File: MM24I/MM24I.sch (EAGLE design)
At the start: 32 parts, among them IC1 SN74LVC2G17DBVR, IC2 SN74LVC14APWR, U1 SN74LVCH16374ADGGR, U2 SN74LVCH16374ADGGR, U3 CY14B104M, U4 SN74AHCT16373DGGR, U5 TLV803SDBZ

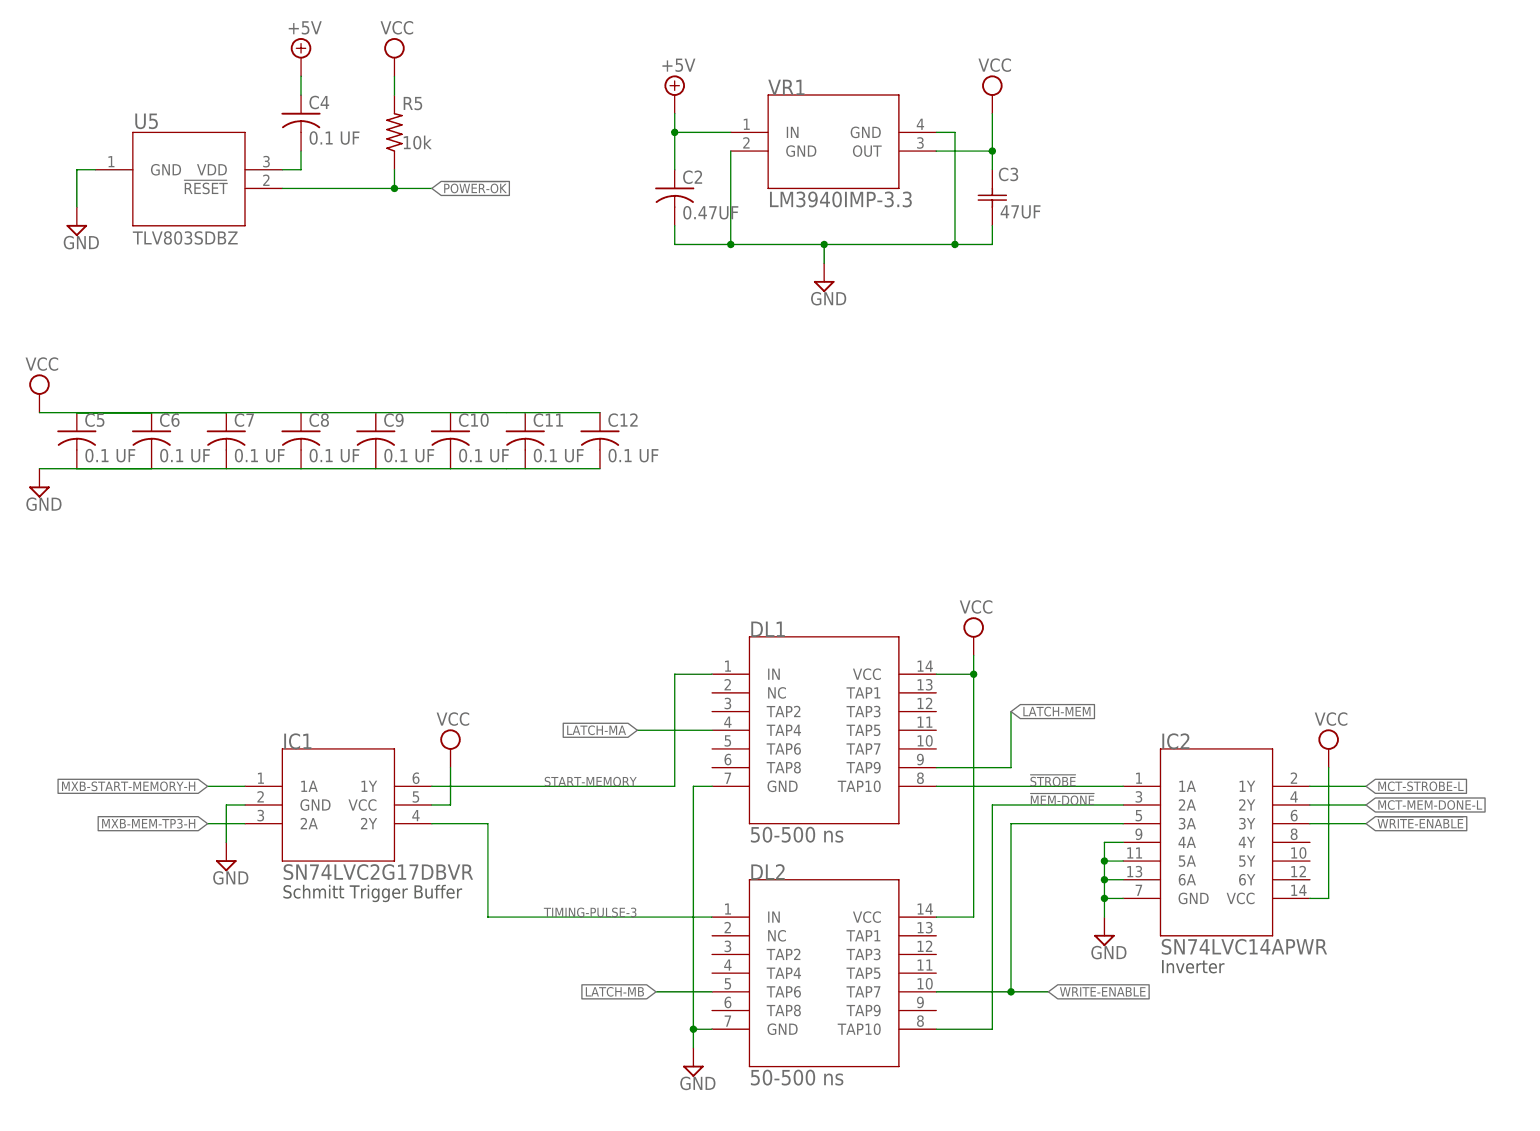
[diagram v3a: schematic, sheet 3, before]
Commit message: Added bypass capacitors, reworked W021J
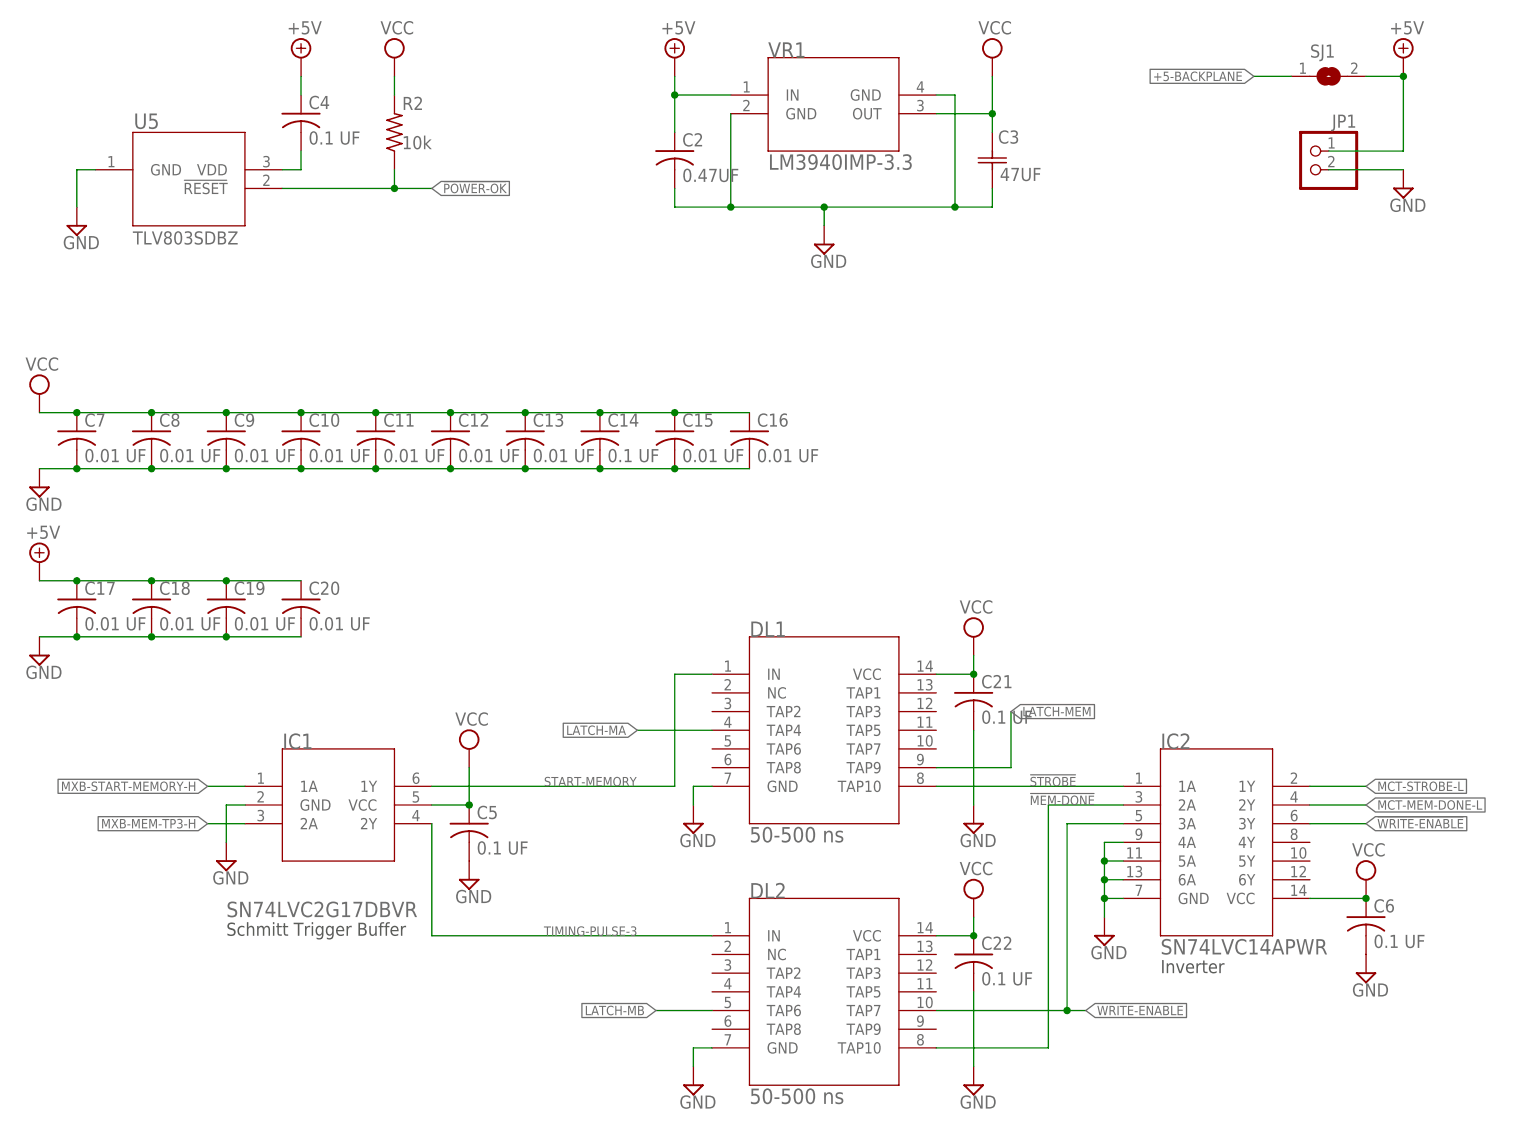
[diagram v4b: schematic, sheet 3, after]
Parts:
- removed R3, R4, R5: 10k, rcl:R-US_R1206
- added C13, C15, C16, C17, C18, C19, C20: 0.01 UF, rcl:C-USC0402
- added C14, C21, C22: 0.1 UF, rcl:C-USC0402
- added JP1: (no value), pinhead:PINHD-1X2
- added SJ1: (no value), jumper:SJ
- C10, C11, C12, C7, C8, C9: value 0.1 UF -> 0.01 UF; device rcl:C-USC0805 -> rcl:C-USC0402
- C4, C5, C6: device rcl:C-USC0805 -> rcl:C-USC0402
- R1, R2: device rcl:R-US_R1206 -> rcl:R-US_R0402
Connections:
- removed net N$10: R2.2, U3.DQ14
- removed net N$12: R3.2, U3.DQ13
- removed net N$8: R4.2, U3.DQ12
- new net +5-BACKPLANE: SJ1.1, U$1A2.1
- net !POWER-OK: now also R2.1; no longer R5.1
- net +5V: now also C17.1, C18.1, C19.1, C20.1, JP1.1, SJ1.2
- net GND: now also C13.2, C14.2, C15.2, C16.2, C17.2, C18.2, C19.2, C20.2, C21.2, C22.2, JP1.2; no longer R2.1, R3.1, R4.1
- net N$9: now also U3.DQ12, U3.DQ13, U3.DQ14
- net VCC: now also C13.1, C14.1, C15.1, C16.1, C21.1, C22.1, R2.2; no longer R5.2
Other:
- moved on the sheet: C10, C11, C12, C2, C3, C5, C6, C7, C8, C9, DL2, VR1

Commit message: Rework MM24I voltage supervisor
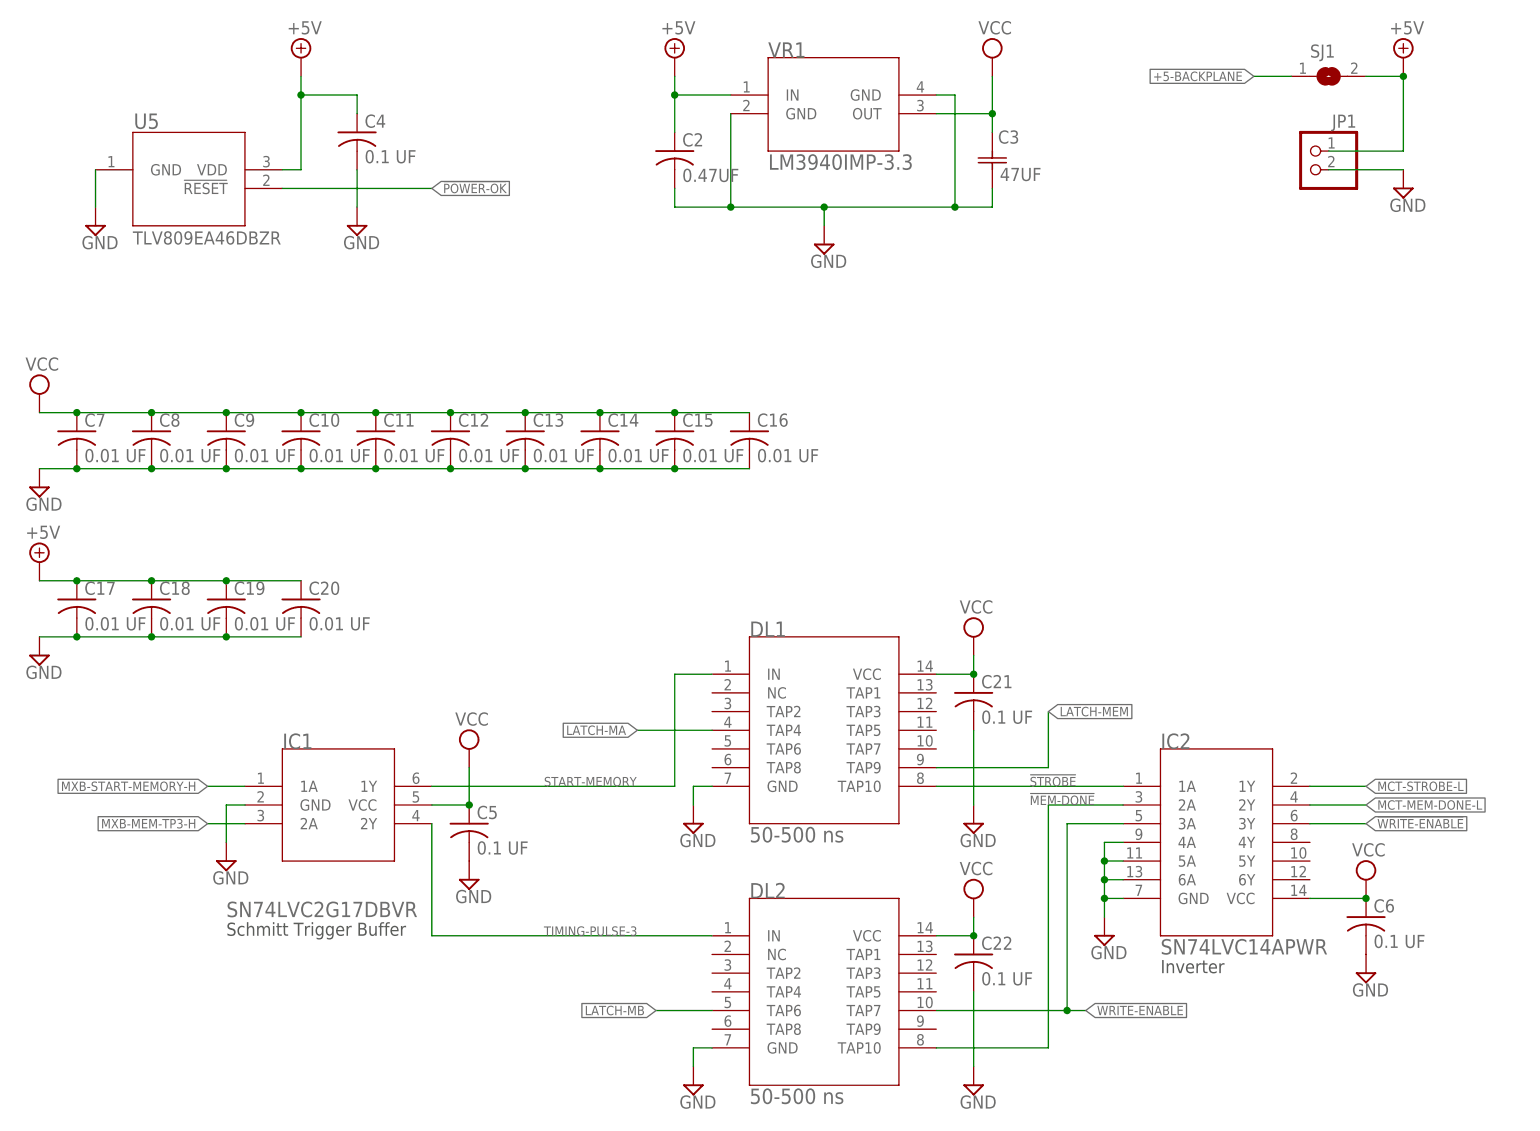
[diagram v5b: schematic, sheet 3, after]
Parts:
- removed R2: 10k, rcl:R-US_R0402
- C14: value 0.1 UF -> 0.01 UF
- U5: value TLV803SDBZ -> TLV809EA46DBZR; device MM24I:TLV803SDBZ -> MM24I:TLV809EA46DBZR
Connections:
- removed net N$1: C4.2, U5.VDD
- net !POWER-OK: no longer R2.1
- net +5V: now also U5.VDD
- net GND: now also C4.2
- net VCC: no longer R2.2
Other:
- moved on the sheet: C4
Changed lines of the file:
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@@
 <part name="U$1" library="dec-con" deviceset="SINGLE" device=""/>
 <part name="SUPPLY23" library="supply2" library_urn="urn:adsk.eagle:library:372" deviceset="GND" device=""/>
-<part name="SUPPLY27" library="supply2" library_urn="urn:adsk.eagle:library:372" deviceset="VCC" device=""/>
-<part name="U5" library="MM24I" deviceset="TLV803SDBZ" device=""/>
-<part name="R2" library="rcl" library_urn="urn:adsk.eagle:library:334" deviceset="R-US_" device="R0402" package3d_urn="urn:adsk.eagle:package:23547/3" value="10k"/>
+<part name="U5" library="MM24I" deviceset="TLV809EA46DBZR" device=""/>
 <part name="SUPPLY28" library="supply2" library_urn="urn:adsk.eagle:library:372" deviceset="+5V" device=""/>
 <part name="C4" library="rcl" library_urn="urn:adsk.eagle:library:334" deviceset="C-US" device="C0402" package3d_urn="urn:adsk.eagle:package:23626/2" value="0.1 UF"/>
@@
 <part name="C12" library="rcl" library_urn="urn:adsk.eagle:library:334" deviceset="C-US" device="C0402" package3d_urn="urn:adsk.eagle:package:23626/2" value="0.01 UF"/>
 <part name="C13" library="rcl" library_urn="urn:adsk.eagle:library:334" deviceset="C-US" device="C0402" package3d_urn="urn:adsk.eagle:package:23626/2" value="0.01 UF"/>
-<part name="C14" library="rcl" library_urn="urn:adsk.eagle:library:334" deviceset="C-US" device="C0402" package3d_urn="urn:adsk.eagle:package:23626/2" value="0.1 UF"/>
+<part name="C14" library="rcl" library_urn="urn:adsk.eagle:library:334" deviceset="C-US" device="C0402" package3d_urn="urn:adsk.eagle:package:23626/2" value="0.01 UF"/>
 <part name="SJ1" library="jumper" library_urn="urn:adsk.eagle:library:252" deviceset="SJ" device="" package3d_urn="urn:adsk.eagle:package:15471/1"/>
 <part name="SUPPLY31" library="supply2" library_urn="urn:adsk.eagle:library:372" deviceset="+5V" device=""/>
@@
 <part name="SUPPLY39" library="supply2" library_urn="urn:adsk.eagle:library:372" deviceset="GND" device=""/>
 <part name="SUPPLY40" library="supply2" library_urn="urn:adsk.eagle:library:372" deviceset="GND" device=""/>
+<part name="SUPPLY27" library="supply2" library_urn="urn:adsk.eagle:library:372" deviceset="GND" device=""/>
 </parts>
 <sheets>
@@
 <attribute name="NAME" x="168.402" y="163.576" size="1.778" layer="95" ratio="10" rot="SR0"/>
 </instance>
-<instance part="SUPPLY23" gate="GND" x="43.18" y="152.4" smashed="yes">
-<attribute name="VALUE" x="41.275" y="149.225" size="1.778" layer="96"/>
-</instance>
-<instance part="SUPPLY27" gate="G$1" x="86.36" y="175.26" smashed="yes">
-<attribute name="VALUE" x="84.455" y="178.435" size="1.778" layer="96"/>
+<instance part="SUPPLY23" gate="GND" x="45.72" y="152.4" smashed="yes">
+<attribute name="VALUE" x="43.815" y="149.225" size="1.778" layer="96"/>
 </instance>
 <instance part="U5" gate="A" x="43.18" y="160.02" smashed="yes">
@@
 <attribute name="VALUE" x="50.8" y="149.86" size="1.778" layer="96"/>
 </instance>
-<instance part="R2" gate="G$1" x="86.36" y="165.1" smashed="yes" rot="R90">
-<attribute name="NAME" x="87.4014" y="168.148" size="1.778" layer="95"/>
-<attribute name="VALUE" x="87.376" y="162.814" size="1.778" layer="96"/>
-</instance>
 <instance part="SUPPLY28" gate="+5V" x="73.66" y="175.26" smashed="yes">
 <attribute name="VALUE" x="71.755" y="178.435" size="1.778" layer="96"/>
 </instance>
-<instance part="C4" gate="G$1" x="73.66" y="167.64" smashed="yes">
-<attribute name="NAME" x="74.676" y="168.275" size="1.778" layer="95"/>
-<attribute name="VALUE" x="74.676" y="163.449" size="1.778" layer="96"/>
+<instance part="C4" gate="G$1" x="81.28" y="165.1" smashed="yes">
+<attribute name="NAME" x="82.296" y="165.735" size="1.778" layer="95"/>
+<attribute name="VALUE" x="82.296" y="160.909" size="1.778" layer="96"/>
 </instance>
 <instance part="SUPPLY29" gate="G$1" x="38.1" y="129.54" smashed="yes">
@@
 <instance part="SUPPLY40" gate="GND" x="165.1" y="35.56" smashed="yes">
 <attribute name="VALUE" x="163.195" y="32.385" size="1.778" layer="96"/>
+</instance>
+<instance part="SUPPLY27" gate="GND" x="81.28" y="152.4" smashed="yes">
+<attribute name="VALUE" x="79.375" y="149.225" size="1.778" layer="96"/>
 </instance>
 </instances>
@@
 <segment>
 <pinref part="SUPPLY23" gate="GND" pin="GND"/>
-<wire x1="45.72" y1="160.02" x2="43.18" y2="160.02" width="0.1524" layer="91"/>
-<wire x1="43.18" y1="160.02" x2="43.18" y2="154.94" width="0.1524" layer="91"/>
+<wire x1="45.72" y1="160.02" x2="45.72" y2="154.94" width="0.1524" layer="91"/>
 <pinref part="U5" gate="A" pin="GND"/>
 </segment>
@@
 <wire x1="165.1" y1="38.1" x2="165.1" y2="48.26" width="0.1524" layer="91"/>
 </segment>
+<segment>
+<pinref part="SUPPLY27" gate="GND" pin="GND"/>
+<pinref part="C4" gate="G$1" pin="2"/>
+<wire x1="81.28" y1="154.94" x2="81.28" y2="160.02" width="0.1524" layer="91"/>
+</segment>
 </net>
 <net name="VCC" class="1">
@@
 <wire x1="160.02" y1="167.64" x2="167.64" y2="167.64" width="0.1524" layer="91"/>
 <junction x="167.64" y="167.64"/>
-</segment>
-<segment>
-<pinref part="R2" gate="G$1" pin="2"/>
-<pinref part="SUPPLY27" gate="G$1" pin="VCC"/>
-<wire x1="86.36" y1="170.18" x2="86.36" y2="172.72" width="0.1524" layer="91"/>
 </segment>
 <segment>
@@
 <segment>
 <pinref part="DL1" gate="A" pin="TAP9"/>
-<wire x1="160.02" y1="78.74" x2="170.18" y2="78.74" width="0.1524" layer="91"/>
-<label x="170.18" y="86.36" size="1.27" layer="95" xref="yes"/>
-<wire x1="170.18" y1="78.74" x2="170.18" y2="86.36" width="0.1524" layer="91"/>
+<wire x1="160.02" y1="78.74" x2="175.26" y2="78.74" width="0.1524" layer="91"/>
+<label x="175.26" y="86.36" size="1.27" layer="95" xref="yes"/>
+<wire x1="175.26" y1="78.74" x2="175.26" y2="86.36" width="0.1524" layer="91"/>
 </segment>
 </net>
@@
 <wire x1="124.46" y1="170.18" x2="132.08" y2="170.18" width="0.1524" layer="91"/>
 <junction x="124.46" y="170.18"/>
-</segment>
-<segment>
-<pinref part="SUPPLY28" gate="+5V" pin="+5V"/>
-<wire x1="73.66" y1="170.18" x2="73.66" y2="172.72" width="0.1524" layer="91"/>
-<pinref part="C4" gate="G$1" pin="1"/>
 </segment>
 <segment>
@@
 <junction x="43.18" y="104.14"/>
 </segment>
-</net>
-<net name="!POWER-OK" class="0">
-<segment>
-<pinref part="U5" gate="A" pin="!RESET"/>
-<wire x1="71.12" y1="157.48" x2="86.36" y2="157.48" width="0.1524" layer="91"/>
-<label x="91.44" y="157.48" size="1.27" layer="95" xref="yes"/>
-<pinref part="R2" gate="G$1" pin="1"/>
-<wire x1="86.36" y1="157.48" x2="91.44" y2="157.48" width="0.1524" layer="91"/>
-<wire x1="86.36" y1="160.02" x2="86.36" y2="157.48" width="0.1524" layer="91"/>
-<junction x="86.36" y="157.48"/>
-</segment>
-</net>
-<net name="N$1" class="1">
 <segment>
 <wire x1="71.12" y1="160.02" x2="73.66" y2="160.02" width="0.1524" layer="91"/>
 <pinref part="U5" gate="A" pin="VDD"/>
-<wire x1="73.66" y1="160.02" x2="73.66" y2="162.56" width="0.1524" layer="91"/>
-<pinref part="C4" gate="G$1" pin="2"/>
-</segment>
-</net>
+<pinref part="SUPPLY28" gate="+5V" pin="+5V"/>
+<wire x1="73.66" y1="172.72" x2="73.66" y2="170.18" width="0.1524" layer="91"/>
+<pinref part="C4" gate="G$1" pin="1"/>
+<wire x1="73.66" y1="170.18" x2="73.66" y2="160.02" width="0.1524" layer="91"/>
+<wire x1="73.66" y1="170.18" x2="81.28" y2="170.18" width="0.1524" layer="91"/>
+<wire x1="81.28" y1="170.18" x2="81.28" y2="167.64" width="0.1524" layer="91"/>
+<junction x="73.66" y="170.18"/>
+</segment>
+</net>
+<net name="!POWER-OK" class="0">
+<segment>
+<pinref part="U5" gate="A" pin="!RESET"/>
+<wire x1="71.12" y1="157.48" x2="91.44" y2="157.48" width="0.1524" layer="91"/>
+<label x="91.44" y="157.48" size="1.27" layer="95" xref="yes"/>
+</segment>
+</net>

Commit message: Disable thermals on pours to work around EAGLE bug
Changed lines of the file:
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@@
-</segment>
-<segment>
-<pinref part="SUPPLY32" gate="GND" pin="GND"/>
-<pinref part="JP1" gate="G$1" pin="2"/>
-<wire x1="223.52" y1="160.02" x2="213.36" y2="160.02" width="0.1524" layer="91"/>
 </segment>
 <segment>
@@
 <wire x1="81.28" y1="154.94" x2="81.28" y2="160.02" width="0.1524" layer="91"/>
 </segment>
+<segment>
+<pinref part="JP1" gate="G$1" pin="2"/>
+<pinref part="SUPPLY32" gate="GND" pin="GND"/>
+<wire x1="213.36" y1="160.02" x2="223.52" y2="160.02" width="0.1524" layer="91"/>
+</segment>
 </net>
